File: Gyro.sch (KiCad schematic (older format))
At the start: 4 parts, among them U7 MPU-6000

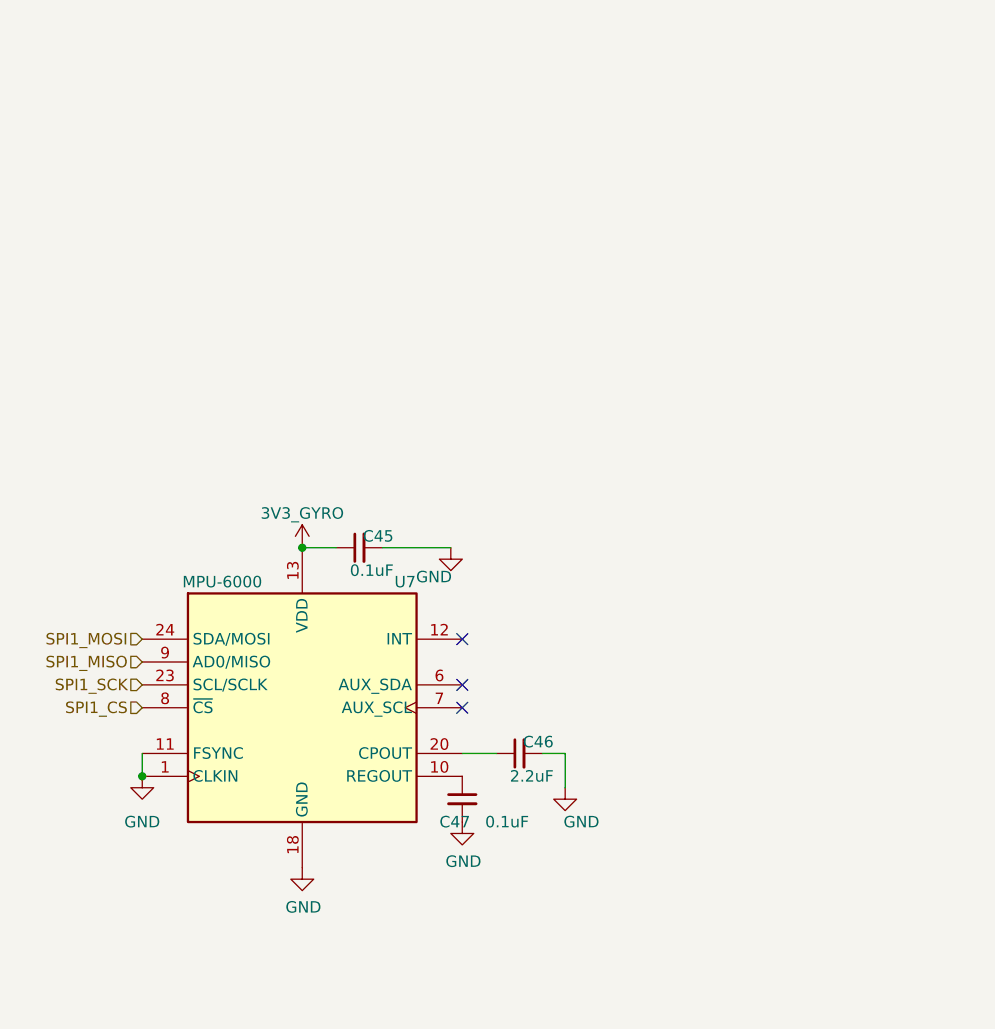
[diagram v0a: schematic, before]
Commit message: Updated the schematics to include pictures
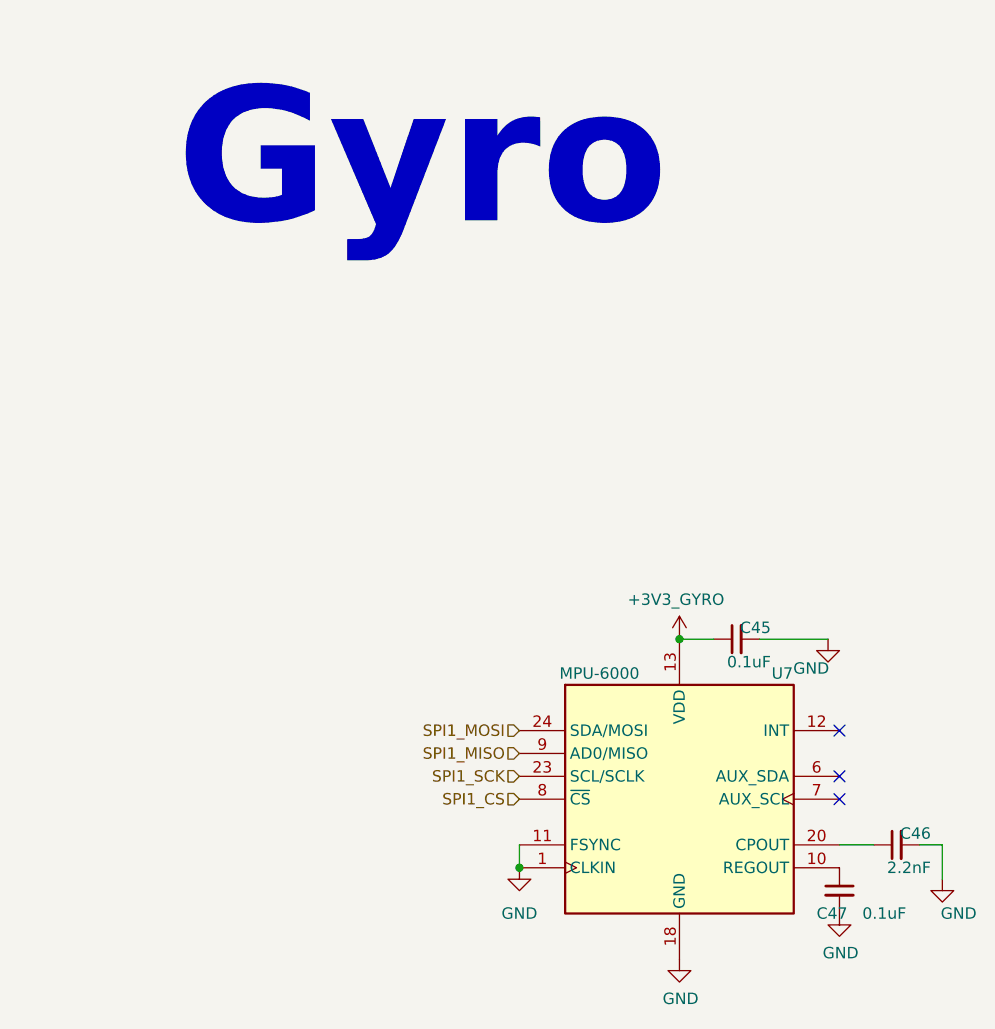
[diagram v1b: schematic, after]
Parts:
- C46: value 2.2uF -> 2.2nF
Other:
- note added: "Gyro"
- moved on the sheet: C45, C46, C47, U7
